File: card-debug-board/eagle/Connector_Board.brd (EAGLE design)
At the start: 69.9 x 34.3 mm, 26 parts, among them J1 ORESAT-DEBUG-CONNECTOR-CARD, J3 USB_A_SMT_FEMALE, U1 FT230XS-R

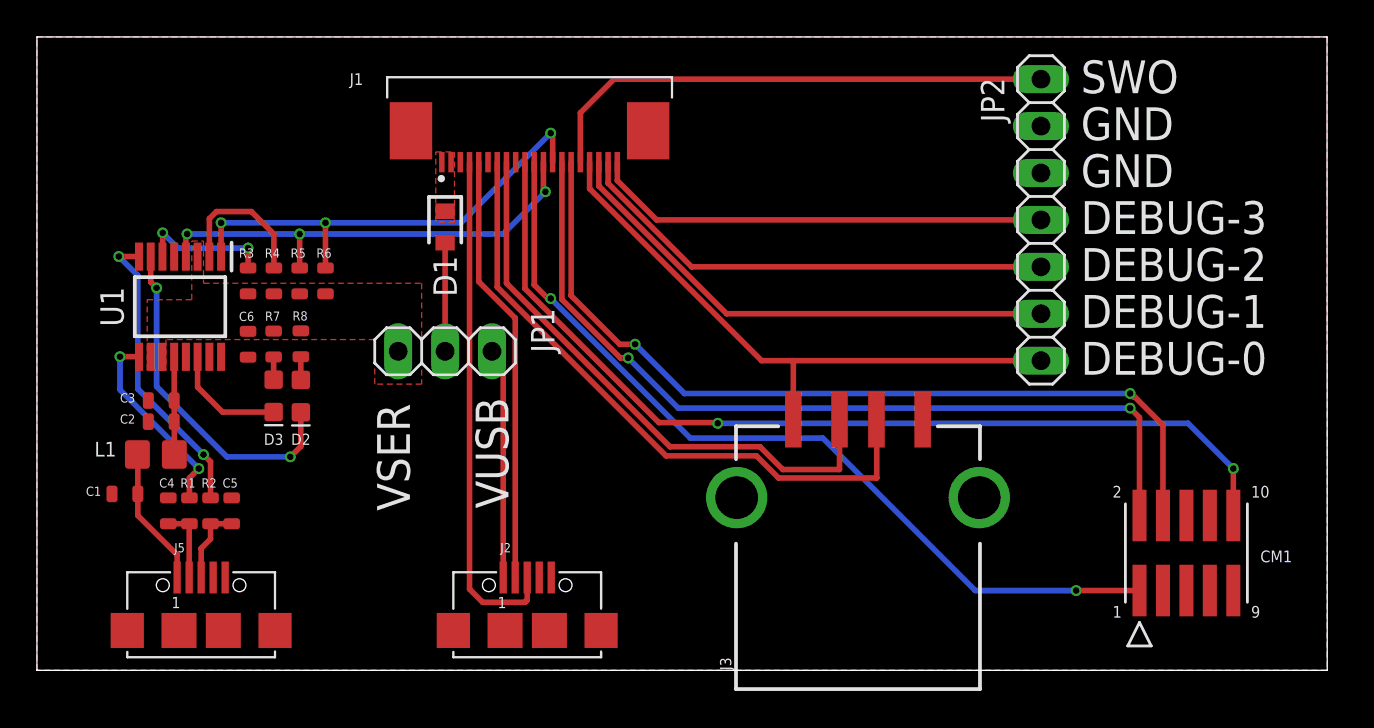
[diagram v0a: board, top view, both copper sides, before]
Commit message: Added lables, diff pairs , GND vias
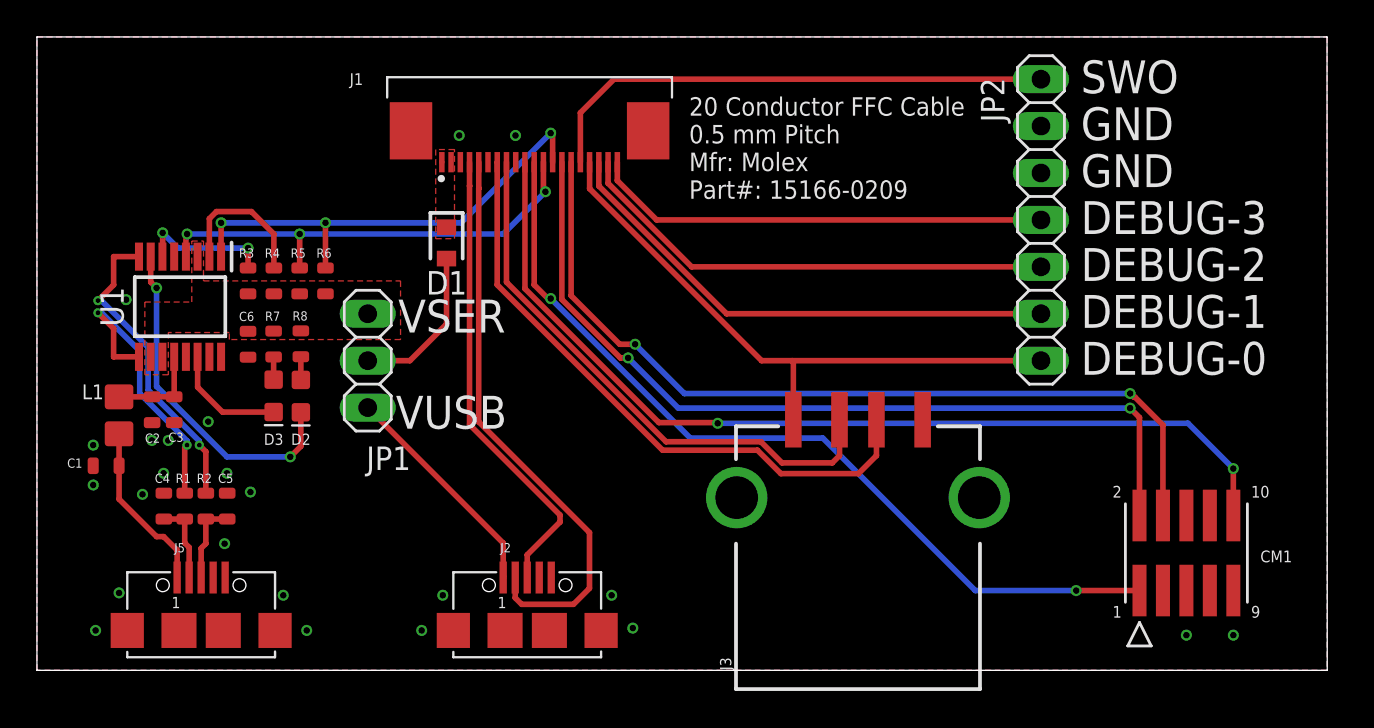
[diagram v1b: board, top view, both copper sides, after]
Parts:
- moved JP1 4.22 mm to (17.9, 16.8), turned to 270 degrees
- moved L1 2.91 mm to (4.45, 13.8), turned to 270 degrees
- moved C1 1.83 mm to (3.75, 11.1)
- moved D1 0.87 mm to (22.2, 23.1)
- moved C3 0.86 mm to (7.43, 14.1), turned to 270 degrees
- moved C2 0.82 mm to (6.24, 14.1), turned to 270 degrees
- moved R1 0.36 mm to (8.00, 8.89)
- moved R2 0.36 mm to (9.14, 8.89)
- moved C5 0.35 mm to (10.3, 8.89)
- moved C4 0.35 mm to (6.87, 8.89)
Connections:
- net D+ renamed D_P
- net D- renamed D_N
- net HOSTD_- renamed HOSTD_N
- net HOST_D+ renamed HOSTD_P
- net SLAVE_D+ renamed SLAVE_D_P
- net SLAVE_D- renamed SLAVE_D_N
- net USBDM renamed USBD_N
- net USBDP renamed USBD_P
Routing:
- net SLAVE_D_N: track 23.3 -> 31.2 mm
- net USBD_N: track 10.7 -> 16.1 mm
- net VBUS_OUT: track 5.88 -> 8.63 mm
- net SLAVE_D_P: track 27.8 -> 25.3 mm
- net N$1: track 7.55 -> 9.31 mm
- net HOSTD_P: track 34.7 -> 33.7 mm
- net USBD_P: track 16.2 -> 17.1 mm
- net HOSTD_N: track 31.4 -> 30.7 mm
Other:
- board text added: "20 Conductor FFC Cable 0.5 mm Pitch Mfr: Molex Part#: 15166-0209"

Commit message: Added P Channel  MOSFET switched VUSB
Made Voltage buses wider
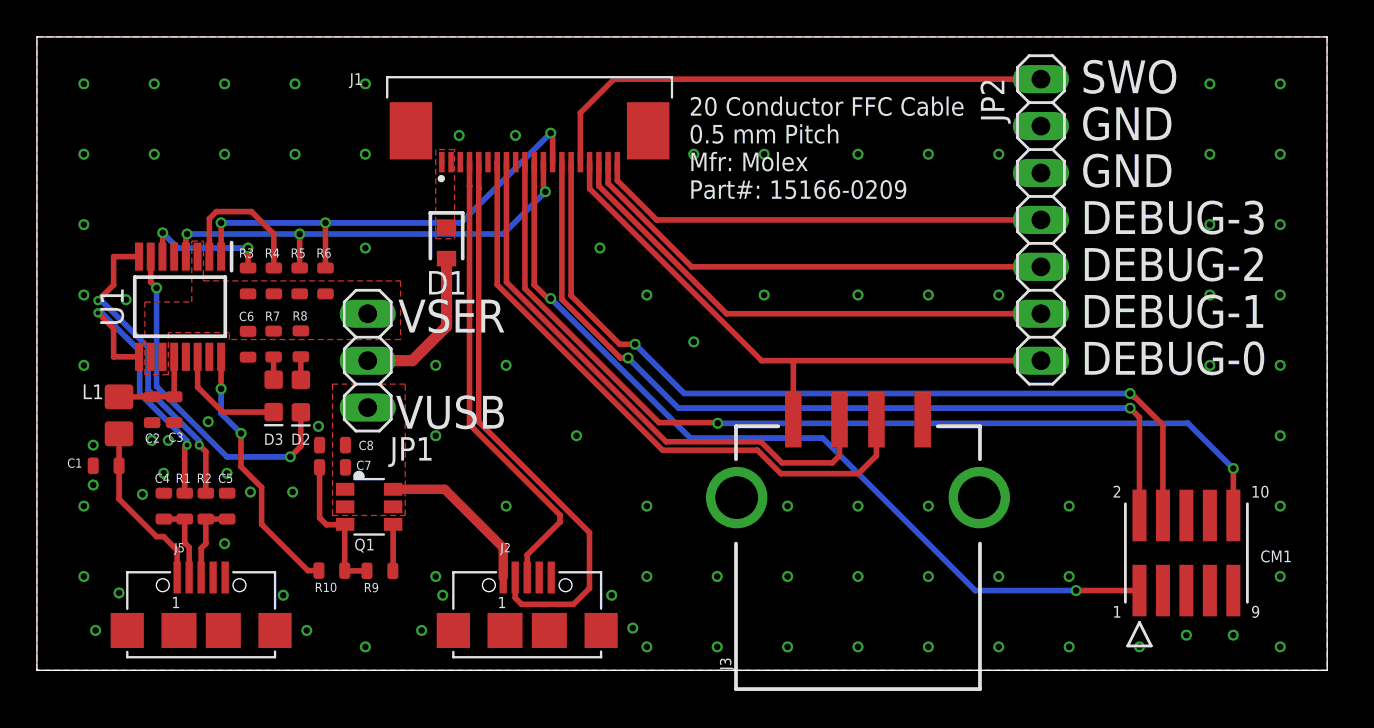
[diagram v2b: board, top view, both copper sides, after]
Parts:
- added C7, C8: 100nF, oresat-rcl:.0603-C-NOSILK
- added Q1: MOSFET-PCH-SOT23-6, Q-MOSFET-PCH-SOT23-6:SOT23-6
- added R10: 1k, oresat-rcl:.0603-C-NOSILK
- added R9: 100k, oresat-rcl:.0603-C-NOSILK
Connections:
- net 5V renamed DEBUG-0/HOST5V
- new net N$3: C7.2, Q1.3, R10.1, R9.1
- new net PWREN#: R10.2, U1.16
- net GND: now also C8.2
- net VCC: now also Q1.4, R9.2
- net VUSB: now also C7.1, C8.1, Q1.1, Q1.2, Q1.5, Q1.6
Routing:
- net PWREN#: track 0.00 -> 14.1 mm, vias 0 -> 2
- net N$3: track 0.00 -> 7.99 mm
- net VUSB: track 12.2 -> 8.92 mm
- net VCC: track 5.15 -> 7.68 mm
- added copper zone on layer 1, net VUSB

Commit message: Added jumper select for Host5V or Debug-0
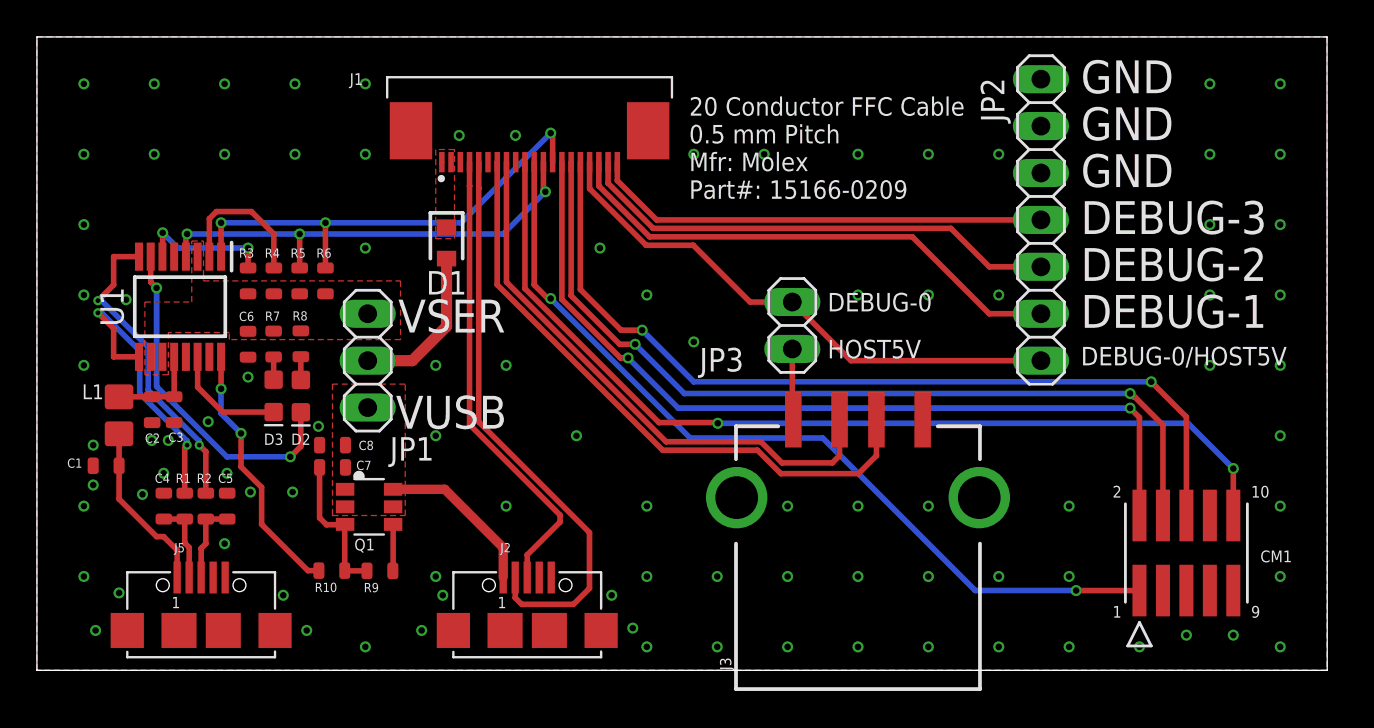
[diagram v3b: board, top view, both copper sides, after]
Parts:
- added JP3: (no value), pinhead:1X02
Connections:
- new net N$2: J3.VBUS, JP3.1
- net DEBUG-0/HOST5V: now also JP3.2; no longer J3.VBUS
- net GND: now also JP2.7
- net SWO: now also CM1.6; no longer JP2.7
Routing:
- net SWO: track 28.4 -> 47.9 mm, vias 0 -> 2
- net N$2: track 0.00 -> 3.86 mm
- net DEBUG-0/HOST5V: track 33.0 -> 29.7 mm
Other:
- board text added: "DEBUG-0/HOST5V"
- board text added: "HOST5V"
- board text removed: "SWO"
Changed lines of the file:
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@@
 <drawing>
 <settings>
-<setting alwaysvectorfont="yes"/>
+<setting alwaysvectorfont="no"/>
 <setting verticaltext="up"/>
 </settings>
-<grid distance="1.27" unitdist="mm" unit="mm" style="lines" multiple="1" display="yes" altdistance="0.0127" altunitdist="mm" altunit="mm"/>
+<grid distance="0.127" unitdist="mm" unit="mm" style="lines" multiple="1" display="yes" altdistance="0.0127" altunitdist="mm" altunit="mm"/>
 <layers>
 <layer number="1" name="Top" color="4" fill="1" visible="yes" active="yes"/>
@@
 <text x="19.431" y="13.081" size="1.778" layer="21">VUSB</text>
 <text x="19.558" y="18.288" size="1.778" layer="21">VSER</text>
-<text x="56.515" y="31.242" size="1.778" layer="21">SWO</text>
+<text x="56.515" y="31.242" size="1.778" layer="21">GND</text>
 <text x="56.515" y="28.702" size="1.778" layer="21">GND</text>
 <text x="56.515" y="26.162" size="1.778" layer="21">GND</text>
@@
 <text x="56.515" y="21.082" size="1.778" layer="21">DEBUG-2</text>
 <text x="56.515" y="18.542" size="1.778" layer="21">DEBUG-1</text>
-<text x="56.515" y="16.002" size="1.778" layer="21">DEBUG-0</text>
+<text x="56.515" y="16.51" size="1" layer="21">DEBUG-0/HOST5V</text>
 <text x="35.306" y="25.527" size="1" layer="21">20 Conductor FFC Cable
 0.5 mm Pitch
 Mfr: Molex
 Part#: 15166-0209</text>
+<text x="42.799" y="16.891" size="1" layer="21">HOST5V</text>
+<text x="42.799" y="19.431" size="1" layer="21">DEBUG-0</text>
 </plain>
 <attributes>
@@
 <attribute name="VALUE" x="17.002" y="13.742" size="0.8" layer="27" font="vector" ratio="15" rot="R180"/>
 </element>
+<element name="JP3" library="pinhead" library_urn="urn:adsk.eagle:library:325" package="1X02" package3d_urn="urn:adsk.eagle:package:22435/2" value="" x="40.894" y="18.669" smashed="yes" rot="R90">
+<attribute name="NAME" x="35.8648" y="16.1798" size="1.27" layer="25" ratio="10"/>
+<attribute name="POPULARITY" value="98" x="40.894" y="18.669" size="1.778" layer="27" rot="R90" display="off"/>
+<attribute name="VALUE" x="44.069" y="16.129" size="1.27" layer="27" rot="R90"/>
+</element>
 </elements>
 <signals>
@@
 <via x="44.45" y="20.32" extent="1-16" drill="0.35"/>
 <via x="48.26" y="20.32" extent="1-16" drill="0.35"/>
-<via x="39.37" y="20.32" extent="1-16" drill="0.35"/>
 <via x="39.37" y="27.94" extent="1-16" drill="0.35"/>
 <via x="35.56" y="27.94" extent="1-16" drill="0.35"/>
@@
 <via x="40.64" y="8.89" extent="1-16" drill="0.35"/>
 <via x="48.26" y="8.89" extent="1-16" drill="0.35"/>
+<contactref element="JP2" pad="7"/>
+<via x="11.43" y="15.875" extent="1-16" drill="0.35"/>
 <wire x1="67.31" y1="27.94" x2="67.31" y2="31.75" width="0" layer="19" extent="1-1"/>
 <wire x1="63.5" y1="31.75" x2="67.31" y2="31.75" width="0" layer="19" extent="1-1"/>
@@
 <wire x1="3.048" y1="12.192" x2="3.0465" y2="11.0744" width="0" layer="19" extent="1-1"/>
 <wire x1="2.54" y1="8.89" x2="3.048" y2="10.033" width="0" layer="19" extent="1-1"/>
+<wire x1="11.43" y1="15.875" x2="9.271" y2="13.462" width="0" layer="19" extent="1-1"/>
+<wire x1="11.43" y1="16.953" x2="11.43" y2="15.875" width="0" layer="19" extent="1-1"/>
 <wire x1="33.02" y1="8.89" x2="33.02" y2="5.08" width="0" layer="19" extent="1-1"/>
 <wire x1="36.83" y1="1.27" x2="36.83" y2="5.08" width="0" layer="19" extent="1-1"/>
-<wire x1="11.43" y1="16.953" x2="9.271" y2="13.462" width="0" layer="19" extent="1-1"/>
 <wire x1="2.54" y1="16.51" x2="3.048" y2="12.192" width="0" layer="19" extent="1-1"/>
 <wire x1="2.54" y1="20.32" x2="2.54" y2="16.51" width="0" layer="19" extent="1-1"/>
@@
 <wire x1="33.02" y1="20.32" x2="30.48" y2="22.86" width="0" layer="19" extent="1-1"/>
 <wire x1="35.56" y1="17.78" x2="33.02" y2="20.32" width="0" layer="19" extent="1-1"/>
-<wire x1="39.37" y1="20.32" x2="35.56" y2="17.78" width="0" layer="19" extent="1-1"/>
-<wire x1="44.45" y1="20.32" x2="39.37" y2="20.32" width="0" layer="19" extent="1-1"/>
-<wire x1="48.26" y1="20.32" x2="44.45" y2="20.32" width="0" layer="19" extent="1-1"/>
+<wire x1="48.26" y1="20.32" x2="47.95" y2="13.562" width="0" layer="19" extent="1-1"/>
 <wire x1="52.07" y1="20.32" x2="48.26" y2="20.32" width="0" layer="19" extent="1-1"/>
+<wire x1="44.45" y1="20.32" x2="48.26" y2="20.32" width="0" layer="19" extent="1-1"/>
 <wire x1="33.09" y1="29.21" x2="30.48" y2="22.86" width="0" layer="19" extent="1-1"/>
 <wire x1="35.56" y1="27.94" x2="33.09" y2="29.21" width="0" layer="19" extent="1-1"/>
@@
 <wire x1="54.356" y1="26.924" x2="52.07" y2="27.94" width="0" layer="19" extent="1-1"/>
 <wire x1="54.356" y1="29.464" x2="54.356" y2="26.924" width="0" layer="19" extent="1-1"/>
+<wire x1="54.356" y1="32.004" x2="54.356" y2="29.464" width="0" layer="19" extent="1-1"/>
 </signal>
 <signal name="VUSB">
@@
 <contactref element="JP2" pad="1"/>
 <contactref element="J1" pad="17"/>
-<contactref element="J3" pad="VBUS"/>
-<wire x1="54.356" y1="16.764" x2="40.894" y2="16.764" width="0.3048" layer="1"/>
-<wire x1="40.894" y1="16.764" x2="39.23141875" y2="16.764" width="0.3048" layer="1"/>
+<contactref element="JP3" pad="2"/>
+<wire x1="54.356" y1="16.764" x2="44.069" y2="16.764" width="0.3048" layer="1"/>
+<wire x1="44.069" y1="16.764" x2="40.894" y2="19.939" width="0.3048" layer="1"/>
+<wire x1="40.894" y1="19.939" x2="38.608" y2="19.939" width="0.3048" layer="1"/>
+<wire x1="38.608" y1="19.939" x2="35.5346" y2="23.0124" width="0.3048" layer="1"/>
 <wire x1="29.92" y1="26.07541875" x2="29.92" y2="27.51" width="0.3048" layer="1"/>
-<wire x1="39.23141875" y1="16.764" x2="29.92" y2="26.07541875" width="0.3048" layer="1"/>
-<wire x1="40.95" y1="13.562" x2="40.95" y2="16.708" width="0.3048" layer="1"/>
-<wire x1="40.95" y1="16.708" x2="40.894" y2="16.764" width="0.3048" layer="1"/>
+<wire x1="35.5346" y1="23.0124" x2="32.98301875" y2="23.0124" width="0.3048" layer="1"/>
+<wire x1="32.98301875" y1="23.0124" x2="29.92" y2="26.07541875" width="0.3048" layer="1"/>
 </signal>
 <signal name="DEBUG-1">
 <contactref element="JP2" pad="2"/>
 <contactref element="J1" pad="18"/>
-<wire x1="54.356" y1="19.304" x2="37.338" y2="19.304" width="0.3048" layer="1"/>
+<wire x1="54.356" y1="19.304" x2="51.562" y2="19.304" width="0.3048" layer="1"/>
+<wire x1="51.562" y1="19.304" x2="47.3964" y2="23.4696" width="0.3048" layer="1"/>
 <wire x1="30.42" y1="26.222" x2="30.42" y2="27.51" width="0.3048" layer="1"/>
-<wire x1="37.338" y1="19.304" x2="30.42" y2="26.222" width="0.3048" layer="1"/>
+<wire x1="47.3964" y1="23.4696" x2="33.1724" y2="23.4696" width="0.3048" layer="1"/>
+<wire x1="33.1724" y1="23.4696" x2="30.42" y2="26.222" width="0.3048" layer="1"/>
 </signal>
 <signal name="DEBUG-2">
 <contactref element="JP2" pad="3"/>
 <contactref element="J1" pad="19"/>
-<wire x1="30.92" y1="27.51" x2="30.92" y2="26.36858125" width="0.3048" layer="1"/>
-<wire x1="35.44458125" y1="21.844" x2="54.356" y2="21.844" width="0.3048" layer="1"/>
-<wire x1="30.92" y1="26.36858125" x2="35.44458125" y2="21.844" width="0.3048" layer="1"/>
+<wire x1="54.356" y1="21.844" x2="51.562" y2="21.844" width="0.3048" layer="1"/>
+<wire x1="51.562" y1="21.844" x2="49.4792" y2="23.9268" width="0.3048" layer="1"/>
+<wire x1="30.92" y1="26.36858125" x2="30.92" y2="27.51" width="0.3048" layer="1"/>
+<wire x1="49.4792" y1="23.9268" x2="33.36178125" y2="23.9268" width="0.3048" layer="1"/>
+<wire x1="33.36178125" y1="23.9268" x2="30.92" y2="26.36858125" width="0.3048" layer="1"/>
 </signal>
 <signal name="DEBUG-3">
@@
 </signal>
 <signal name="SWO">
-<contactref element="JP2" pad="7"/>
 <contactref element="J1" pad="16"/>
-<wire x1="29.42" y1="27.51" x2="29.42" y2="30.182" width="0.3048" layer="1"/>
-<wire x1="31.242" y1="32.004" x2="54.356" y2="32.004" width="0.3048" layer="1"/>
-<wire x1="29.42" y1="30.182" x2="31.242" y2="32.004" width="0.3048" layer="1"/>
+<contactref element="CM1" pad="6"/>
+<wire x1="29.42" y1="27.51" x2="29.42" y2="20.618" width="0.3048" layer="1"/>
+<wire x1="31.623" y1="18.415" x2="32.766" y2="18.415" width="0.3048" layer="1"/>
+<via x="32.766" y="18.415" extent="1-16" drill="0.35"/>
+<wire x1="32.766" y1="18.415" x2="35.56" y2="15.621" width="0.3048" layer="16"/>
+<via x="60.325" y="15.621" extent="1-16" drill="0.35"/>
+<wire x1="60.325" y1="15.621" x2="62.23" y2="13.716" width="0.3048" layer="1"/>
+<wire x1="62.23" y1="13.716" x2="62.23" y2="8.382" width="0.3048" layer="1"/>
+<wire x1="29.42" y1="20.618" x2="31.623" y2="18.415" width="0.3048" layer="1"/>
+<wire x1="35.56" y1="15.621" x2="60.325" y2="15.621" width="0.3048" layer="16"/>
 </signal>
 <signal name="GND_2">
@@
 <wire x1="15.302" y1="8.2565" x2="15.6759" y2="7.8826" width="0.3048" layer="1"/>
 </signal>
+<signal name="N$2">
+<contactref element="J3" pad="VBUS"/>
+<contactref element="JP3" pad="1"/>
+<wire x1="40.894" y1="17.399" x2="40.894" y2="13.618" width="0.3048" layer="1"/>
+<wire x1="40.894" y1="13.618" x2="40.95" y2="13.562" width="0.3048" layer="1"/>
+</signal>
 </signals>
